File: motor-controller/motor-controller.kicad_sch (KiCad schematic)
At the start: 50 parts, among them J1 Motor0, J2 Motor1, J3 BATT, J4 MCU, Q1 2N3904, Q2 2N3904, U1 LT1161

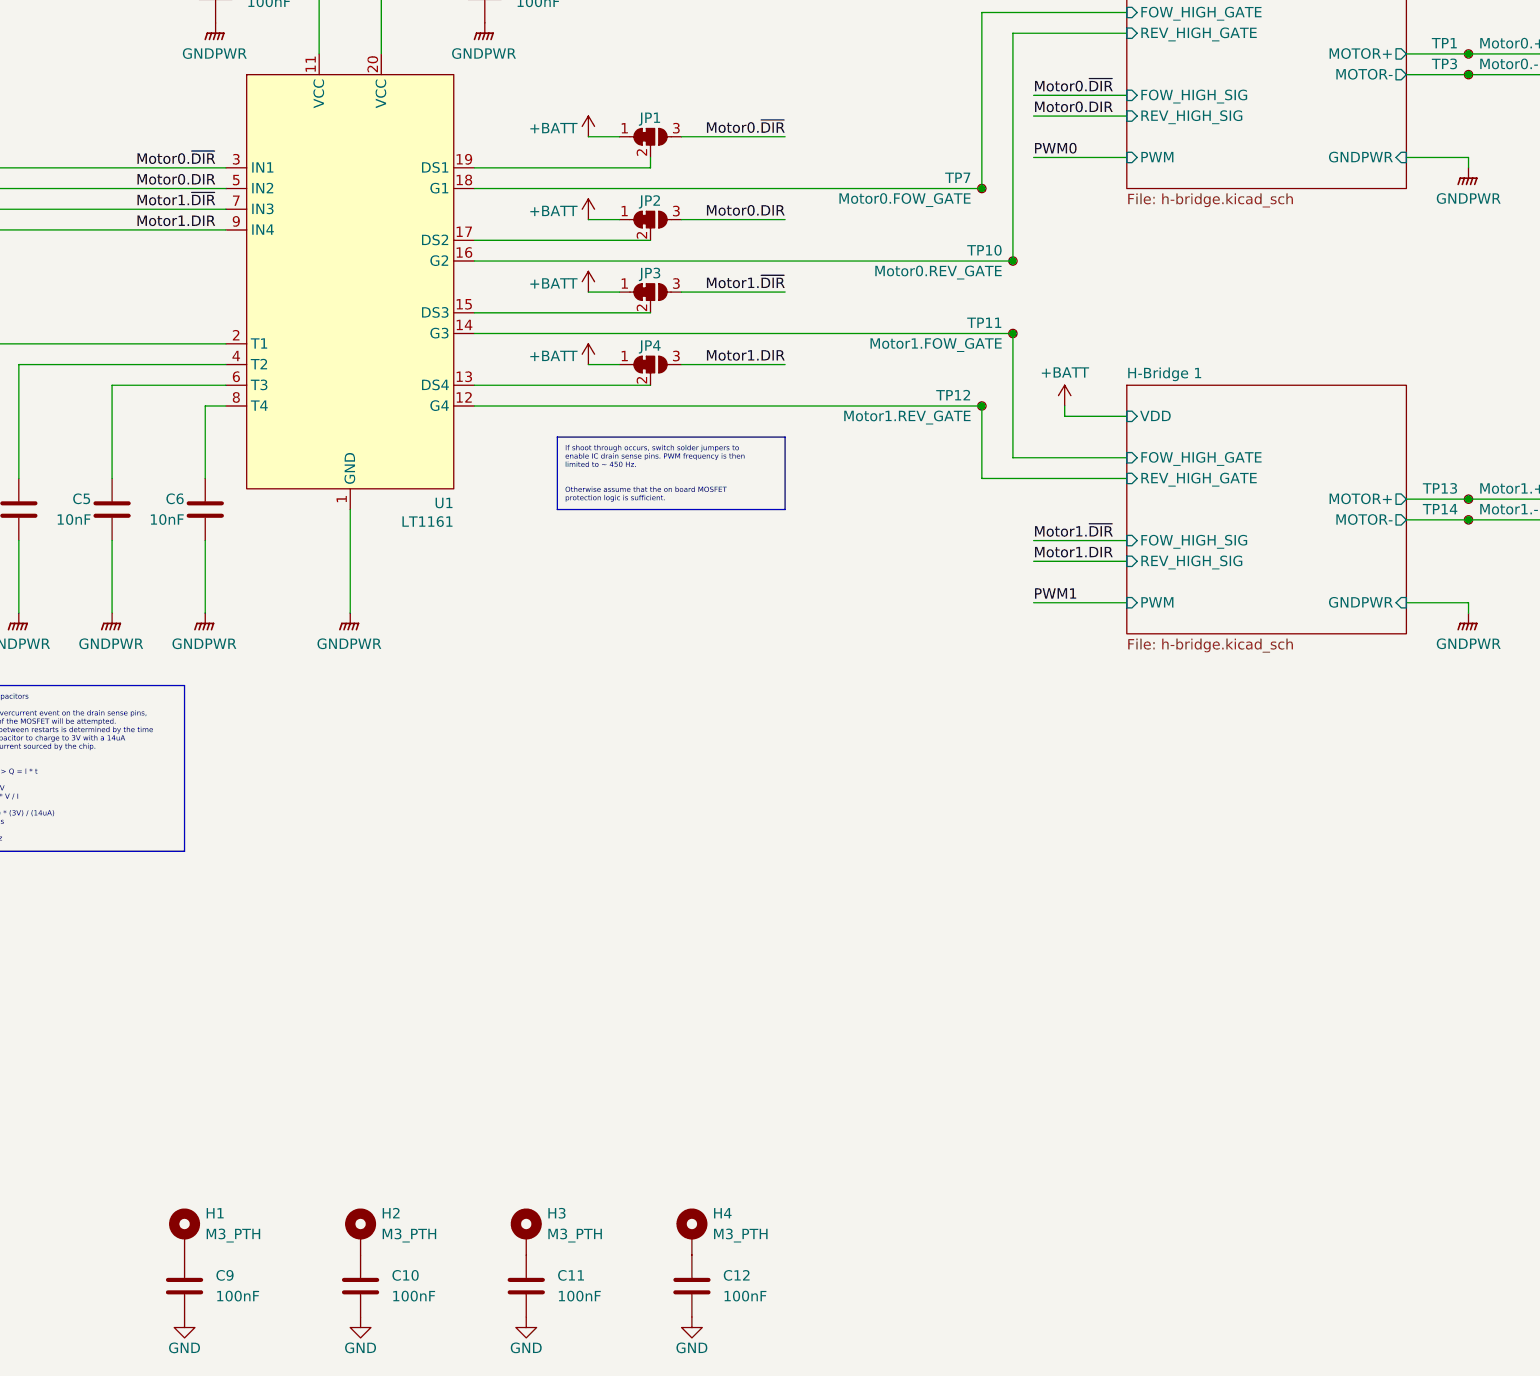
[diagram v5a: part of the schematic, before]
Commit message: Update PWM signal selection to avoid an accidental resistor divider
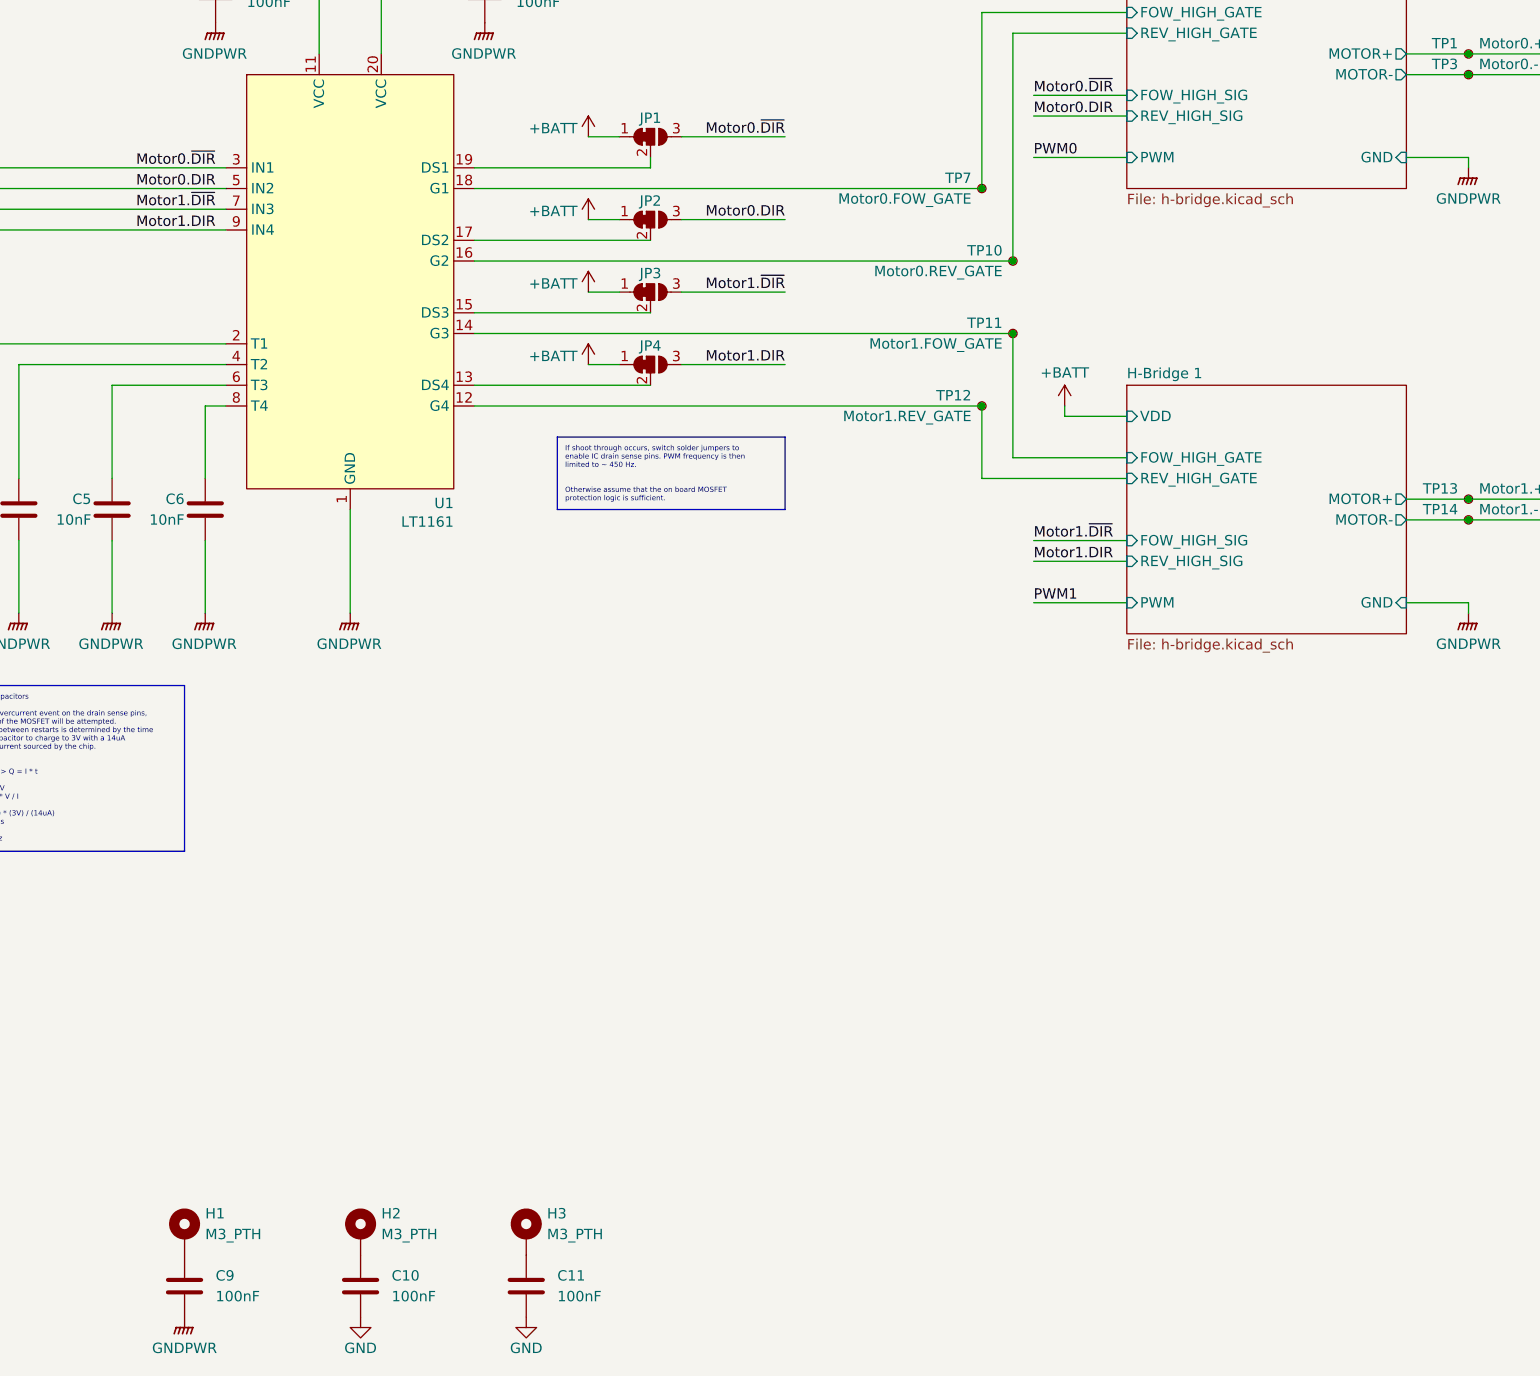
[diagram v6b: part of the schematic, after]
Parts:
- removed C12: 100nF, Capacitor_THT:C_Disc_D3.0mm_W2.0mm_P2.50mm, symbol GS_Capacitor_THT:C_THT_100nF
- removed H4: M3_PTH, MountingHole:MountingHole_3.2mm_M3_Pad, symbol Mechanical:MountingHole_Pad
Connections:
- net GND: no longer C9.2
- net GNDPWR: now also C9.2
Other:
- sheet H-Bridge 0 ports: added GND; removed GNDPWR
- sheet H-Bridge 1 ports: added GND; removed GNDPWR
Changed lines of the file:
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@@
 	)
 	(symbol
-		(lib_id "power:GND")
-		(at 276.86 269.24 0)
-		(unit 1)
-		(exclude_from_sim no)
-		(in_bom yes)
-		(on_board yes)
-		(dnp no)
-		(property "Reference" "#PWR035"
-			(at 276.86 275.59 0)
-			(effects
-				(font
-					(size 1.27 1.27)
-				)
-				(hide yes)
-			)
-		)
-		(property "Value" "GND"
-			(at 276.86 273.05 0)
-			(effects
-				(font
-					(size 1.27 1.27)
-				)
-			)
-		)
-		(property "Footprint" ""
-			(at 276.86 269.24 0)
-			(effects
-				(font
-					(size 1.27 1.27)
-				)
-				(hide yes)
-			)
-		)
-		(property "Datasheet" ""
-			(at 276.86 269.24 0)
-			(effects
-				(font
-					(size 1.27 1.27)
-				)
-				(hide yes)
-			)
-		)
-		(property "Description" "Power symbol creates a global label with name \"GND\" , ground"
-			(at 276.86 269.24 0)
-			(effects
-				(font
-					(size 1.27 1.27)
-				)
-				(hide yes)
-			)
-		)
-		(pin "1"
-		)
-		(instances
-			(project "motor-controller"
-				(path "/3cf627b4-179f-4b19-ad57-a5207e12b14c"
-					(reference "#PWR035")
-					(unit 1)
-				)
-			)
-		)
-	)
-	(symbol
 		(lib_id "power:+BATT")
 		(at 322.58 157.48 0)
@@
 	)
 	(symbol
-		(lib_id "Mechanical:MountingHole_Pad")
-		(at 276.86 259.08 0)
-		(unit 1)
-		(exclude_from_sim no)
-		(in_bom no)
-		(on_board yes)
-		(dnp no)
-		(fields_autoplaced yes)
-		(property "Reference" "H4"
-			(at 279.4 256.5399 0)
-			(effects
-				(font
-					(size 1.27 1.27)
-				)
-				(justify left)
-			)
-		)
-		(property "Value" "M3_PTH"
-			(at 279.4 259.0799 0)
-			(effects
-				(font
-					(size 1.27 1.27)
-				)
-				(justify left)
-			)
-		)
-		(property "Footprint" "MountingHole:MountingHole_3.2mm_M3_Pad"
-			(at 276.86 259.08 0)
-			(effects
-				(font
-					(size 1.27 1.27)
-				)
-				(hide yes)
-			)
-		)
-		(property "Datasheet" "~"
-			(at 276.86 259.08 0)
-			(effects
-				(font
-					(size 1.27 1.27)
-				)
-				(hide yes)
-			)
-		)
-		(property "Description" "Mounting Hole with connection"
-			(at 276.86 259.08 0)
-			(effects
-				(font
-					(size 1.27 1.27)
-				)
-				(hide yes)
-			)
-		)
-		(pin "1"
-		)
-		(instances
-			(project "motor-controller"
-				(path "/3cf627b4-179f-4b19-ad57-a5207e12b14c"
-					(reference "H4")
-					(unit 1)
-				)
-			)
-		)
-	)
-	(symbol
 		(lib_id "Connector:TestPoint_Small")
 		(at 312.42 130.81 0)
@@
 	)
 	(symbol
-		(lib_id "GS_Capacitor_THT:C_THT_100nF")
-		(at 276.86 265.43 0)
-		(unit 1)
-		(exclude_from_sim no)
-		(in_bom yes)
-		(on_board yes)
-		(dnp no)
-		(property "Reference" "C12"
-			(at 280.67 264.1599 0)
-			(effects
-				(font
-					(size 1.27 1.27)
-				)
-				(justify left)
-			)
-		)
-		(property "Value" "100nF"
-			(at 280.67 266.6999 0)
-			(effects
-				(font
-					(size 1.27 1.27)
-				)
-				(justify left)
-			)
-		)
-		(property "Footprint" "Capacitor_THT:C_Disc_D3.0mm_W2.0mm_P2.50mm"
-			(at 276.86 243.078 0)
-			(effects
-				(font
-					(size 1.27 1.27)
-				)
-				(hide yes)
-			)
-		)
-		(property "Datasheet" "~"
-			(at 276.86 251.714 0)
-			(effects
-				(font
-					(size 1.27 1.27)
-				)
-				(hide yes)
-			)
-		)
-		(property "Description" "100nF Unpolarized Capacitor"
-			(at 276.86 249.682 0)
-			(effects
-				(font
-					(size 1.27 1.27)
-				)
-				(hide yes)
-			)
-		)
-		(pin "2"
-		)
-		(pin "1"
-		)
-		(instances
-			(project "motor-controller"
-				(path "/3cf627b4-179f-4b19-ad57-a5207e12b14c"
-					(reference "C12")
-					(unit 1)
-				)
-			)
-		)
-	)
-	(symbol
 		(lib_id "power:GNDPWR")
 		(at 134.62 124.46 0)
@@
 	)
 	(symbol
+		(lib_id "power:GNDPWR")
+		(at 214.63 269.24 0)
+		(unit 1)
+		(exclude_from_sim no)
+		(in_bom yes)
+		(on_board yes)
+		(dnp no)
+		(property "Reference" "#PWR032"
+			(at 214.63 274.32 0)
+			(effects
+				(font
+					(size 1.27 1.27)
+				)
+				(hide yes)
+			)
+		)
+		(property "Value" "GNDPWR"
+			(at 214.63 273.05 0)
+			(effects
+				(font
+					(size 1.27 1.27)
+				)
+			)
+		)
+		(property "Footprint" ""
+			(at 214.63 270.51 0)
+			(effects
+				(font
+					(size 1.27 1.27)
+				)
+				(hide yes)
+			)
+		)
+		(property "Datasheet" ""
+			(at 214.63 270.51 0)
+			(effects
+				(font
+					(size 1.27 1.27)
+				)
+				(hide yes)
+			)
+		)
+		(property "Description" "Power symbol creates a global label with name \"GNDPWR\" , global ground"
+			(at 214.63 269.24 0)
+			(effects
+				(font
+					(size 1.27 1.27)
+				)
+				(hide yes)
+			)
+		)
+		(pin "1"
+		)
+		(instances
+			(project "motor-controller"
+				(path "/3cf627b4-179f-4b19-ad57-a5207e12b14c"
+					(reference "#PWR032")
+					(unit 1)
+				)
+			)
+		)
+	)
+	(symbol
 		(lib_id "Connector:TestPoint_Small")
 		(at 59.69 176.53 0)
@@
 	)
 	(symbol
-		(lib_id "power:GND")
-		(at 214.63 269.24 0)
-		(unit 1)
-		(exclude_from_sim no)
-		(in_bom yes)
-		(on_board yes)
-		(dnp no)
-		(property "Reference" "#PWR032"
-			(at 214.63 275.59 0)
-			(effects
-				(font
-					(size 1.27 1.27)
-				)
-				(hide yes)
-			)
-		)
-		(property "Value" "GND"
-			(at 214.63 273.05 0)
-			(effects
-				(font
-					(size 1.27 1.27)
-				)
-			)
-		)
-		(property "Footprint" ""
-			(at 214.63 269.24 0)
-			(effects
-				(font
-					(size 1.27 1.27)
-				)
-				(hide yes)
-			)
-		)
-		(property "Datasheet" ""
-			(at 214.63 269.24 0)
-			(effects
-				(font
-					(size 1.27 1.27)
-				)
-				(hide yes)
-			)
-		)
-		(property "Description" "Power symbol creates a global label with name \"GND\" , ground"
-			(at 214.63 269.24 0)
-			(effects
-				(font
-					(size 1.27 1.27)
-				)
-				(hide yes)
-			)
-		)
-		(pin "1"
-		)
-		(instances
-			(project "motor-controller"
-				(path "/3cf627b4-179f-4b19-ad57-a5207e12b14c"
-					(reference "#PWR032")
-					(unit 1)
-				)
-			)
-		)
-	)
-	(symbol
 		(lib_id "GS_Gate_Drivers:LT1161")
 		(at 234.95 142.24 0)
@@
 			)
 		)
-		(pin "GNDPWR" input
+		(pin "GND" input
 			(at 364.49 181.61 0)
 			(effects
@@
 			)
 		)
-		(pin "GNDPWR" input
+		(pin "GND" input
 			(at 364.49 127 0)
 			(effects

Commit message: Finish layout
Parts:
- removed TP1: Motor0.+, TestPoint:TestPoint_Pad_1.5x1.5mm, symbol Connector:TestPoint_Small
- removed TP13: Motor1.+, TestPoint:TestPoint_Pad_1.5x1.5mm, symbol Connector:TestPoint_Small
- removed TP14: Motor1.-, TestPoint:TestPoint_Pad_1.5x1.5mm, symbol Connector:TestPoint_Small
- removed TP15: MCU.PWM1, TestPoint:TestPoint_Pad_1.5x1.5mm, symbol Connector:TestPoint_Small
- removed TP16: MCU.DIR1, TestPoint:TestPoint_Pad_1.5x1.5mm, symbol Connector:TestPoint_Small
- removed TP2: MCU.PWM0, TestPoint:TestPoint_Pad_1.5x1.5mm, symbol Connector:TestPoint_Small
- removed TP3: Motor0.-, TestPoint:TestPoint_Pad_1.5x1.5mm, symbol Connector:TestPoint_Small
- removed TP4: MCU.DIR0, TestPoint:TestPoint_Pad_1.5x1.5mm, symbol Connector:TestPoint_Small
- added C12: 100nF, Capacitor_THT:C_Disc_D3.0mm_W2.0mm_P2.50mm, symbol GS_Capacitor_THT:C_THT_100nF
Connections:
- net +BATT: now also C12.1
- net GNDPWR: now also C12.2
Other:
- moved on the sheet: TP19

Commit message: Generate schematic pdf
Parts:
- added S1: Logo, GS_Virtual:ENPH253_Logo_Small, symbol GS_Virtual:ENPH253_Logo
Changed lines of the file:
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@@
+	)
+	(symbol
+		(lib_id "GS_Virtual:ENPH253_Logo")
+		(at 290.83 279.4 0)
+		(unit 1)
+		(exclude_from_sim no)
+		(in_bom yes)
+		(on_board yes)
+		(dnp no)
+		(fields_autoplaced yes)
+		(property "Reference" "S1"
+			(at 290.83 275.59 0)
+			(effects
+				(font
+					(size 1.27 1.27)
+				)
+			)
+		)
+		(property "Value" "Logo"
+			(at 290.83 271.018 0)
+			(effects
+				(font
+					(size 1.27 1.27)
+				)
+				(hide yes)
+			)
+		)
+		(property "Footprint" "GS_Virtual:ENPH253_Logo_Small"
+			(at 290.83 279.4 0)
+			(effects
+				(font
+					(size 1.27 1.27)
+				)
+				(hide yes)
+			)
+		)
+		(property "Datasheet" ""
+			(at 290.83 279.4 0)
+			(effects
+				(font
+					(size 1.27 1.27)
+				)
+				(hide yes)
+			)
+		)
+		(property "Description" "ENPH 253 Team Logo"
+			(at 290.83 273.304 0)
+			(effects
+				(font
+					(size 1.27 1.27)
+				)
+				(hide yes)
+			)
+		)
+		(instances
+			(project ""
+				(path "/3cf627b4-179f-4b19-ad57-a5207e12b14c"
+					(reference "S1")
+					(unit 1)
+				)
+			)
+		)
 	)
 	(symbol
